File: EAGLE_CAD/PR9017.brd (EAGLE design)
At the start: 70 x 70 mm, 74 parts, among them SW1 C&K_PTS645, Y1 ABS25XTAL

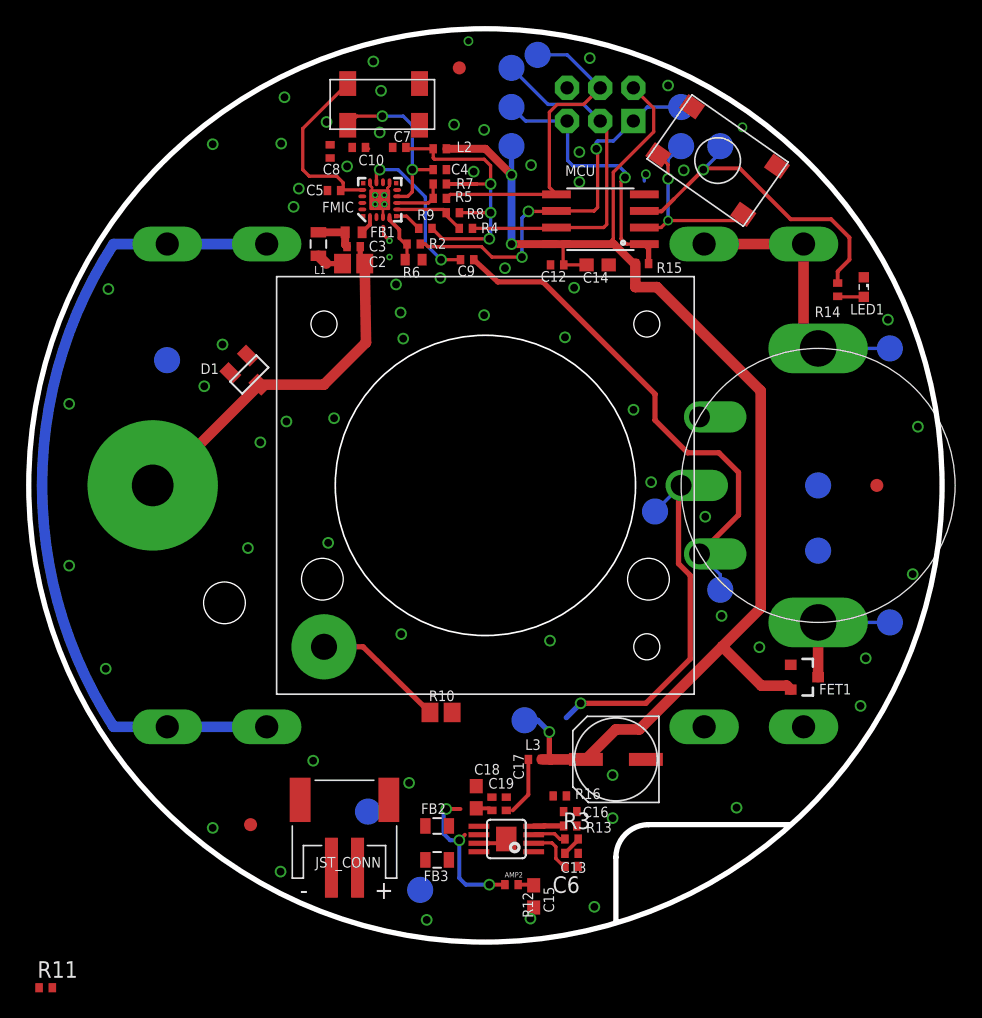
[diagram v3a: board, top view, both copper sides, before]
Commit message: okay, woah
i spent a *ton* of time going through the partlist & BOM. at this point
basically everything in the circuit is from our PR_Parts_Library. i
also simplified & improved the package names, descriptions, etc. and i
gave all the passives 0603 footprints that came from the Common Parts
Library.

big thing: the values @ manufacturer part numbers. all of our parts
have a custom attribute called “MFG_PN”. we should go through EVERY
PART ON OUR SCHEMATIC and put actual manufacturer part numbers in those
fields. i did this for all the parts that seemed critical, but i didn’t
touch passives at all.

there’s also some other stuff that will matter on the BOM/partlist
side, but it’s probably best to just walk through in person or
digitally.

then: i went through all the parts and actually made them 0603.

then: i played with the FMIC area a bit. it’s not perfect but it’s a
start.

then: i started laying out the amp section. that’s definitely not done.
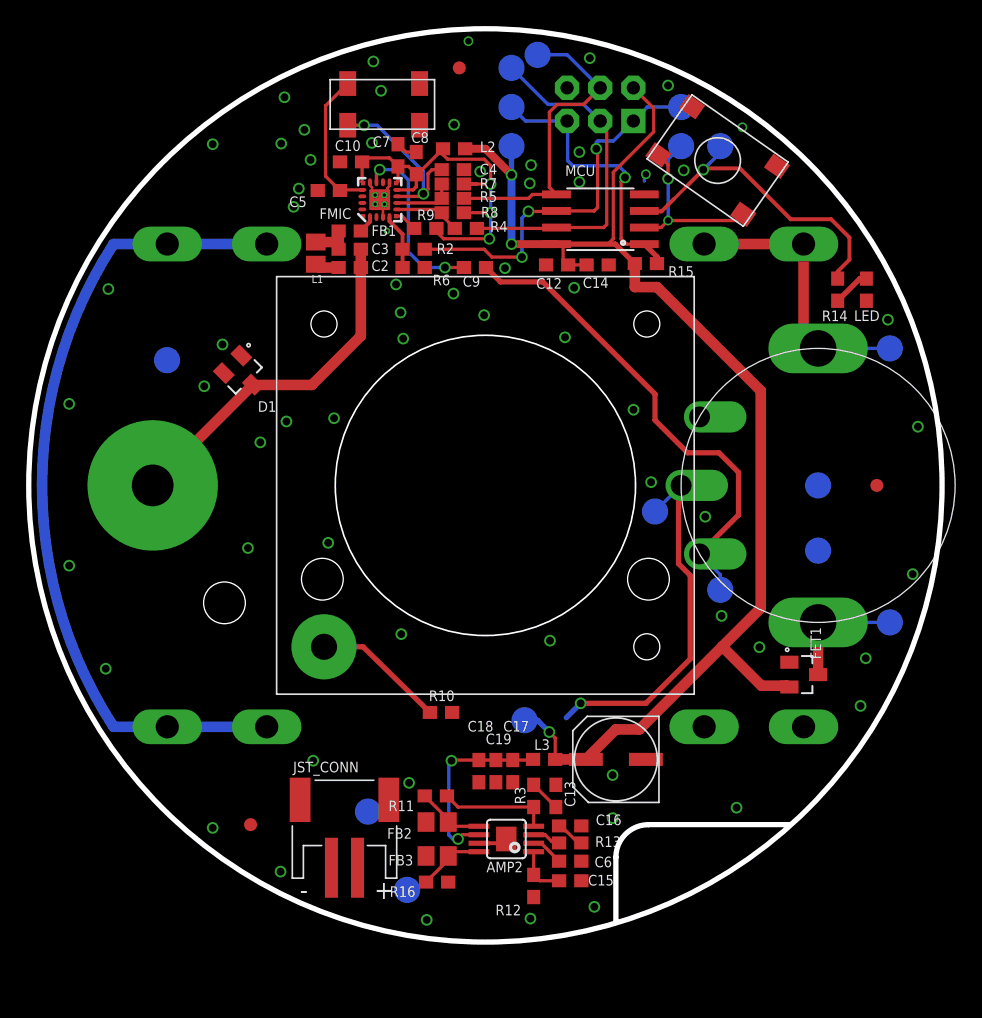
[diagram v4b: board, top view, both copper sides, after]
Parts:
- removed LED1: (no value), led:SML0603
- added LED: LED, PR_Parts_Library:0603_CPL
- AMP2: value TPA6203A1 -> (none); device PR_Parts_Library:POWER-SOP8 -> PR_Parts_Library:8-MSOP
- ANT_MOUNT: value M3_SCREW_POST -> DNP; device PR_Parts_Library:M3_SCREW_POST -> PR_Parts_Library:M3_BOLT_HOLE
- C1: device PR_Parts_Library:NICHICON_SERIESUD -> PR_Parts_Library:NICHICON_UD_63
- C10, C12, C13, C16, C17, C19, C3, C4, C5, C6, C7, C8, C9, L2, L3, R11, R12, R13, R14, R15, R16, R2, R3, R4, R5, R7, R8, R9: device PR_Parts_Library:C0402_WORTHINGTON -> PR_Parts_Library:0603_CPL
- C14, C15, C18: device resistor:C0603 -> PR_Parts_Library:0603_CPL
- C2: value (none) -> DNP; device resistor:C0805 -> PR_Parts_Library:0603_CPL
- D1: device SparkFun-DiscreteSemi:SOT23 -> PR_Parts_Library:SOT23_CPL
- FB1, R6: device resistor:R0402 -> PR_Parts_Library:0603_CPL
- FB2, FB3, L1: device SparkFun-Passives:0805 -> PR_Parts_Library:0805_ADAFRUIT
- FET1: value AO3435 -> (none); device PR_Parts_Library:AO3435 -> PR_Parts_Library:SOT23_CPL
- FMIC: value SI4702 -> (none); device PR_Parts_Library:SI470X -> PR_Parts_Library:SI470X_20_QFN
- ISP: value ISP -> (none); device SparkFun-Connectors:2X3-NS -> PR_Parts_Library:2X3-NS
- JP5, JP6: value BK-92_MPD_AA_BATT_CLIP -> (none); device PR_Parts_Library:BK-92_MPD_AA_BATT_CLIP -> PR_Parts_Library:BK92_AA_BATT
- JST_CONN: device adafruit:JST-PH-2-SMT-RA -> PR_Parts_Library:JST-PH-2-SMT-RA
- MARK1, MARK2, MARK3: value FIDUCIAL -> (none); device adafruit:FIDUCIAL_1MM -> PR_Parts_Library:FIDUCIAL_1MM
- MCU: value Tiny45-20-SMT -> (none); device SparkFun-DigitalIC:SO08-EIAJ -> PR_Parts_Library:8-SOIC
- R1: value RV170SF_TAIWANA_POT_SW -> (none); device PR_Parts_Library:RV170SF_TAIWANA_POT_SW -> PR_Parts_Library:RV170SF_SW_POT
- R10: value (none) -> DNP; device resistor:R0805 -> PR_Parts_Library:0603_CPL
- SPKR_PLACE: value (none) -> DNP; device PR_Parts_Library:CE32A_FOR_JST -> PR_Parts_Library:PR2023_SPKR_PLACE
- SW1: value C&K_PTS645 -> (none); device PR_Parts_Library:C&K_TACTILE_SWITCH -> PR_Parts_Library:C&K_PTS645_SMT
- TP1, TP10, TP11, TP12, TP13, TP14, TP15, TP16, TP17, TP2, TP3, TP4, TP5, TP6, TP7, TP8, TP9: value TPTP20R -> (none); device testpad:TP20R -> PR_Parts_Library:TP20R
- Y1: value ABS25XTAL -> (none); device PR_Parts_Library:ABS25XTAL -> PR_Parts_Library:4-SOJ
- moved R11 33.3 mm to (31.2, 11.2), turned to 180 degrees
- moved R16 11.5 mm to (31.3, 4.60)
- moved C8 6.66 mm to (29.7, 59.7), turned to 90 degrees
- moved C13 4.56 mm to (40.4, 11.2), turned to 270 degrees
- moved R3 4.39 mm to (38.7, 11.2), turned to 90 degrees
- moved C15 3.05 mm to (41.5, 4.70), turned to 0 degrees
- moved C17 2.55 mm to (37.1, 13.1), turned to 270 degrees
- moved C19 2.52 mm to (35.8, 13.1), turned to 270 degrees
- moved C18 2.01 mm to (34.5, 13.1), turned to 270 degrees
- moved R12 1.70 mm to (38.7, 4.30), turned to 270 degrees
- moved R13 1.30 mm to (41.5, 7.60)
- moved C10 1.25 mm to (24.7, 59.8), turned to 180 degrees
- moved L2 1.10 mm to (32.6, 60.8)
- moved C16 1.10 mm to (41.5, 8.90), turned to 180 degrees
- moved C4 1.00 mm to (32.5, 59.2)
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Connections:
- net A_IN: no longer C13.1
- net A_OUT: now also C13.1
- net GND: now also LED.2; no longer LED1.C
- net N$7: now also LED.1; no longer LED1.A
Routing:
- net 3.3V: track 25.7 -> 32.9 mm
- net N$14: track 2.48 -> 8.48 mm
- net N$4: track 0.00 -> 5.23 mm
- net N$11: track 0.00 -> 5.19 mm
- net N$20: track 1.21 -> 3.91 mm
- net N$10: track 13.8 -> 11.1 mm
- net N$2: track 17.2 -> 14.6 mm, vias 3 -> 2
- net N$23: track 0.00 -> 2.24 mm
- net VCC: track 108.3 -> 106.1 mm
- net N$9: track 12.2 -> 13.8 mm
- net SDIO: track 25.6 -> 24.3 mm
- net ANT: track 28.6 -> 27.4 mm
- net N$12: track 3.68 -> 2.52 mm
- net A_IN: track 39.1 -> 37.9 mm
- net N$7: track 2.02 -> 2.90 mm
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
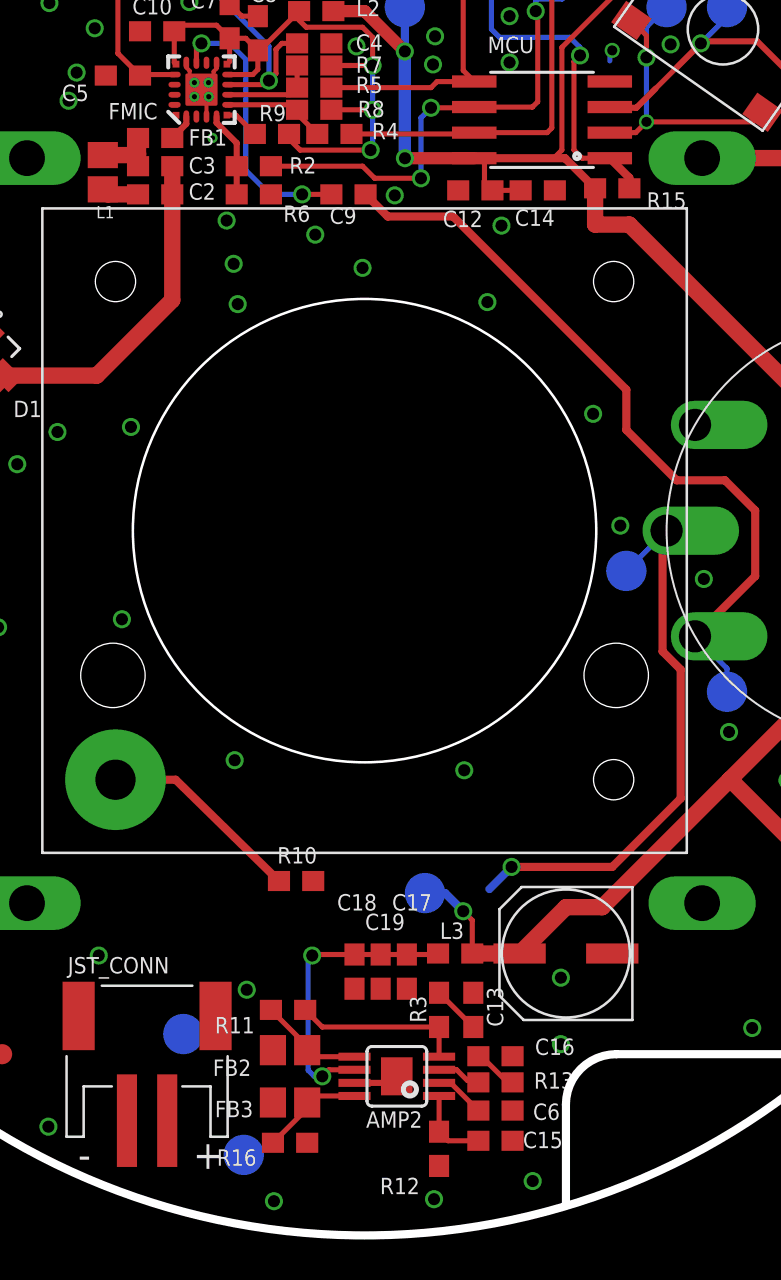
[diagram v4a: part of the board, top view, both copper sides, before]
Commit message: Amp Updates
Changed the layout
-moved the decoupling as close as possible to the vd pin
-kept bypass cap also close by
-rerouted power
-removed the cap to ground on the shutdown pin from out previous
design, was not in place on any of the documentation for the 6203.
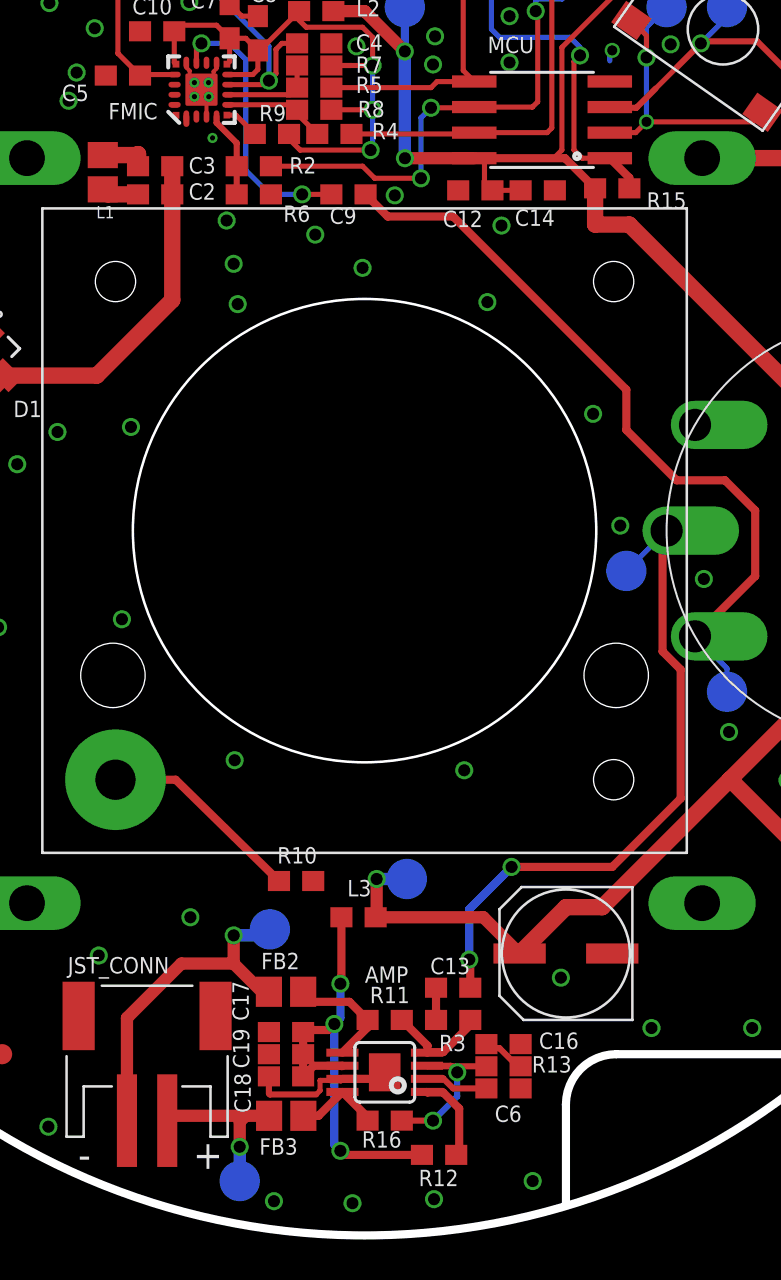
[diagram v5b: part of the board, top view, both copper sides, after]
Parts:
- removed AMP2: (no value), PR_Parts_Library:8-MSOP
- removed C15: 10uF, PR_Parts_Library:0603_CPL
- removed FB1: (no value), PR_Parts_Library:0603_CPL
- added AMP: (no value), PR_Parts_Library:8-MSOP
- moved TP6 6.75 mm to (30.3, 15.2)
- moved C17 6.71 mm to (31.1, 10.1), turned to 180 degrees
- moved C19 6.24 mm to (31.1, 9.00), turned to 180 degrees
- moved C18 6.21 mm to (31.1, 7.90), turned to 180 degrees
- moved L3 5.13 mm to (34.7, 15.8)
- moved R16 4.83 mm to (36.0, 5.70)
- moved R11 4.83 mm to (36.0, 10.7)
- moved FB2 2.91 mm to (31.1, 12.1)
- moved C13 1.49 mm to (39.4, 12.3), turned to 0 degrees
- moved TP7 1.32 mm to (28.8, 2.70)
- moved C6 1.17 mm to (41.9, 7.30)
- moved TP4 1.14 mm to (37.1, 17.7)
- moved R13 0.89 mm to (41.9, 8.40)
- moved R3 0.86 mm to (39.4, 10.7), turned to 180 degrees
- moved C16 0.72 mm to (41.9, 9.50)
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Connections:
- net A_OUT: now also C13.2; no longer C13.1
- net GND: now also AMP.7, AMP.9; no longer AMP2.7, AMP2.9, C15.2
- net N$11: now also AMP.8; no longer AMP2.8
- net N$12: now also AMP.2; no longer AMP2.2
- net N$14: now also AMP.4; no longer AMP2.4
- net N$16: no longer FB1.1
- net N$2: now also AMP.6; no longer AMP2.6
- net N$20: now also AMP.1; no longer AMP2.1, C15.1
- net N$3: now also C13.1; no longer C13.2
- net N$4: now also AMP.5; no longer AMP2.5
- net N$5: now also AMP.3; no longer AMP2.3
- net N$6: no longer FB1.2
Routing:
- net SPK_OUT+: track 0.00 -> 17.8 mm, vias 0 -> 1
- net SPK_OUT-: track 0.00 -> 8.52 mm, vias 0 -> 1
- net N$2: track 14.6 -> 22.4 mm, vias 2 -> 3
- net GND: track 10.4 -> 17.7 mm, vias 68 -> 69
- net N$5: track 2.21 -> 9.04 mm, vias 0 -> 2
- net A_OUT: track 27.9 -> 33.3 mm, vias 1 -> 2
- net VCC: track 106.1 -> 110.5 mm
- net N$14: track 8.48 -> 5.10 mm
- net N$6: track 1.35 -> 0.36 mm
- net N$11: track 5.19 -> 4.37 mm
- net N$3: track 2.40 -> 1.60 mm
- net N$16: track 3.17 -> 2.37 mm
- net N$4: track 5.23 -> 5.95 mm
- net N$12: track 2.52 -> 3.17 mm

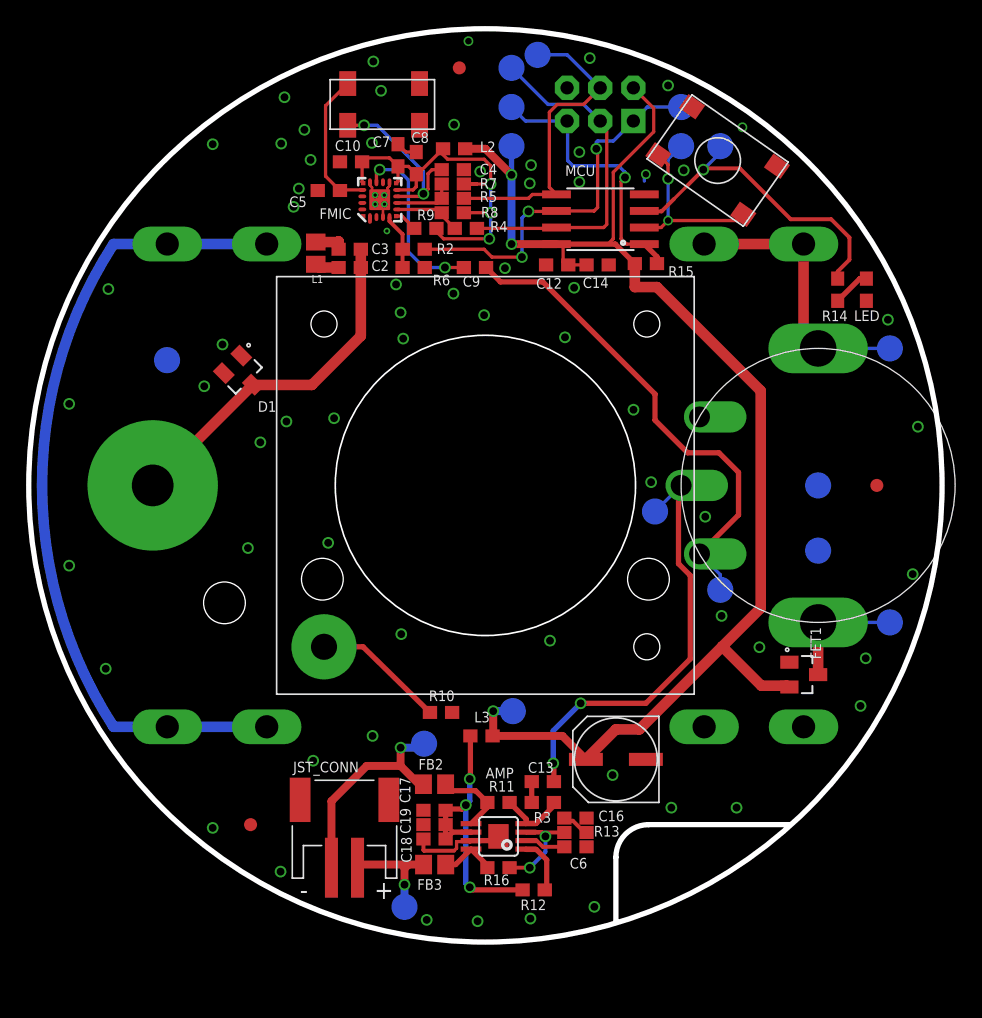
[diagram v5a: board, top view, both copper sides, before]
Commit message: updated all part number etc
part number
added attributes for tolerance, voltage, power, etc
re routed FMIC per AN383
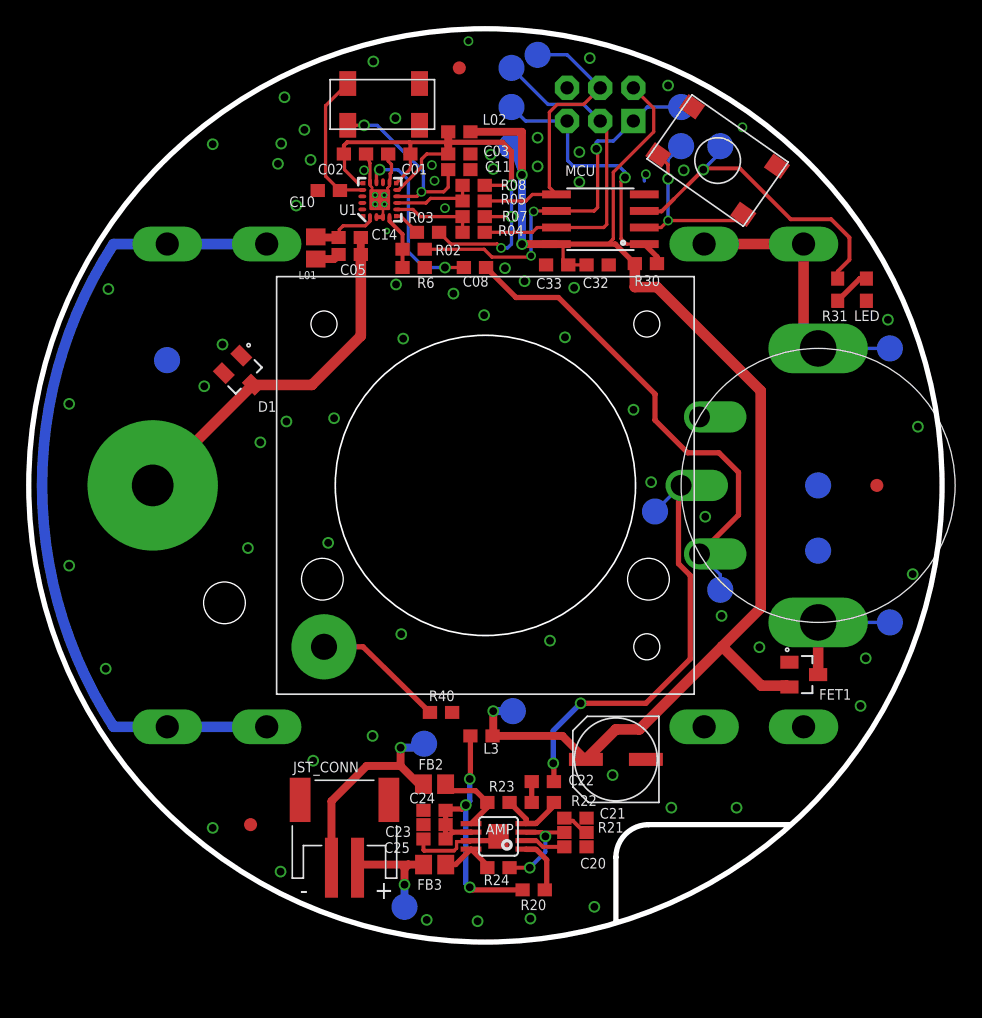
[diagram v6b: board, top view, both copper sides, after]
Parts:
- removed C2: DNP, PR_Parts_Library:0603_CPL
- removed C3: 47p, PR_Parts_Library:0603_CPL
- removed C4: 22pF, PR_Parts_Library:0603_CPL
- removed C5: 22p, PR_Parts_Library:0603_CPL
- removed C7: 22n, PR_Parts_Library:0603_CPL
- removed C8: .1u, PR_Parts_Library:0603_CPL
- removed L1: 180nH, PR_Parts_Library:0805_ADAFRUIT
- removed L2: 2.2k@100MHz, PR_Parts_Library:0603_CPL
- removed R4, R5: 330, PR_Parts_Library:0603_CPL
- removed R7, R8, R9: 4.7k, PR_Parts_Library:0603_CPL
- added C01, C02: 22n, PR_Parts_Library:0603_CPL
- added C03: .1u, PR_Parts_Library:0603_CPL
- added C05: DNP, PR_Parts_Library:0603_CPL
- added C11: 22pF, PR_Parts_Library:0603_CPL
- added C32: 10uF, PR_Parts_Library:0603_CPL
- added L01: 180nH, PR_Parts_Library:0805_ADAFRUIT
- added L02: 2.2k@100MHz, PR_Parts_Library:0603_CPL
- added R03, R07, R08: 4.7k, PR_Parts_Library:0603_CPL
- added R04, R05: 330, PR_Parts_Library:0603_CPL
- C10: value 22n -> 22pF
- C14: value 10uF -> 47p
- moved C14 19.1 mm to (24.6, 54.0), turned to 180 degrees
- moved C10 2.78 mm to (23.0, 57.6)
- renumbered C1 to C40, C12 to C33, C13 to C22, C16 to C21, C17 to C24, C18 to C25, C19 to C23, C6 to C20, C9 to C08, FMIC to U1, R10 to R40, R11 to R23, R12 to R20, R13 to R21, R14 to R31, R15 to R30, R16 to R24, R2 to R02, R3 to R22, Y1 to X1
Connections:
- removed net N$6: U1.2
- net !SEN-L: now also R03.1; no longer R9.1
- net 3.3V: now also C01.1, C02.1, C03.1, L02.2, R03.2, R07.2, R08.2; no longer C10.1, C7.1, C8.1, L2.2, R7.2, R8.2, R9.2
- net ANT: now also C05.1, C14.1; no longer C2.1, C3.1
- net GND: now also C01.2, C02.2, C03.2, C05.2, C11.2, C32.2, L01.2; no longer C14.2, C2.2, C4.2, C5.2, C7.2, C8.2, L1.2
- net N$1: now also C11.1; no longer C4.1
- net N$10: now also C10.1; no longer C5.1
- net N$16: now also C14.2, L01.1, U1.2; no longer C3.2, L1.1
- net SCLK: now also R04.1; no longer R4.1
- net SCLK-L: now also R04.2, R07.1; no longer R4.2, R8.1
- net SDIO: now also R05.1; no longer R5.1
- net SDIO-L: now also R05.2, R08.1; no longer R5.2, R7.1
- net VCC: now also C32.1, L02.1; no longer C14.1, L2.1
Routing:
- net 3.3V: track 32.9 -> 45.2 mm
- net GND: track 17.7 -> 20.9 mm, vias 69 -> 72
- net N$16: track 2.37 -> 5.33 mm
- net VCC: track 110.5 -> 112.8 mm
- net SDIO-L: track 4.66 -> 6.44 mm
- net SDIO: track 24.3 -> 22.8 mm
- net SCLK-L: track 5.47 -> 6.44 mm
- net ANT: track 27.4 -> 28.3 mm
- net N$1: track 13.9 -> 14.4 mm
